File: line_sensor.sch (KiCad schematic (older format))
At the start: 59 parts, among them SW1 SW_DIP_x03, SW2 SW_DIP_x03, SW3 SW_DIP_x03, SW4 SW_DIP_x03, SW5 SW_DIP_x03, SW6 SW_DIP_x03, U1 XH_2, U2 XH_2, U3 XH_2, U4 NJM7800SDL1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

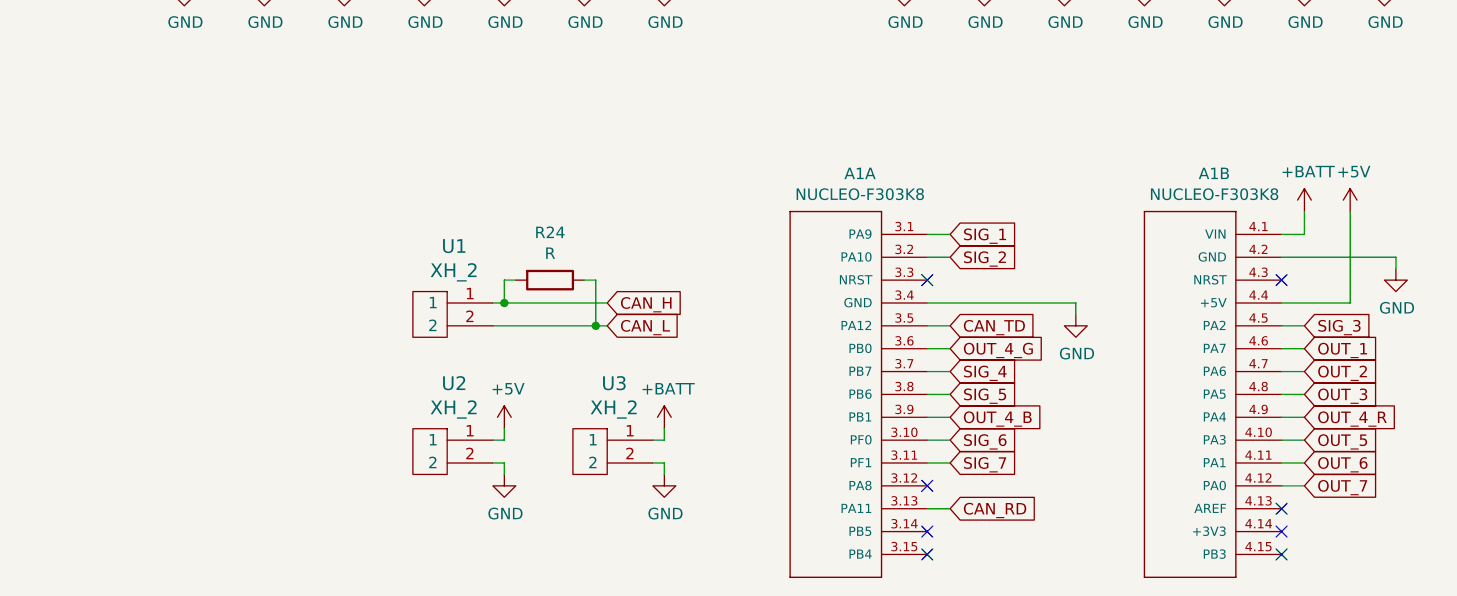
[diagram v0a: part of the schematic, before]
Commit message: update: ライブラリ関係を統合，リネーム
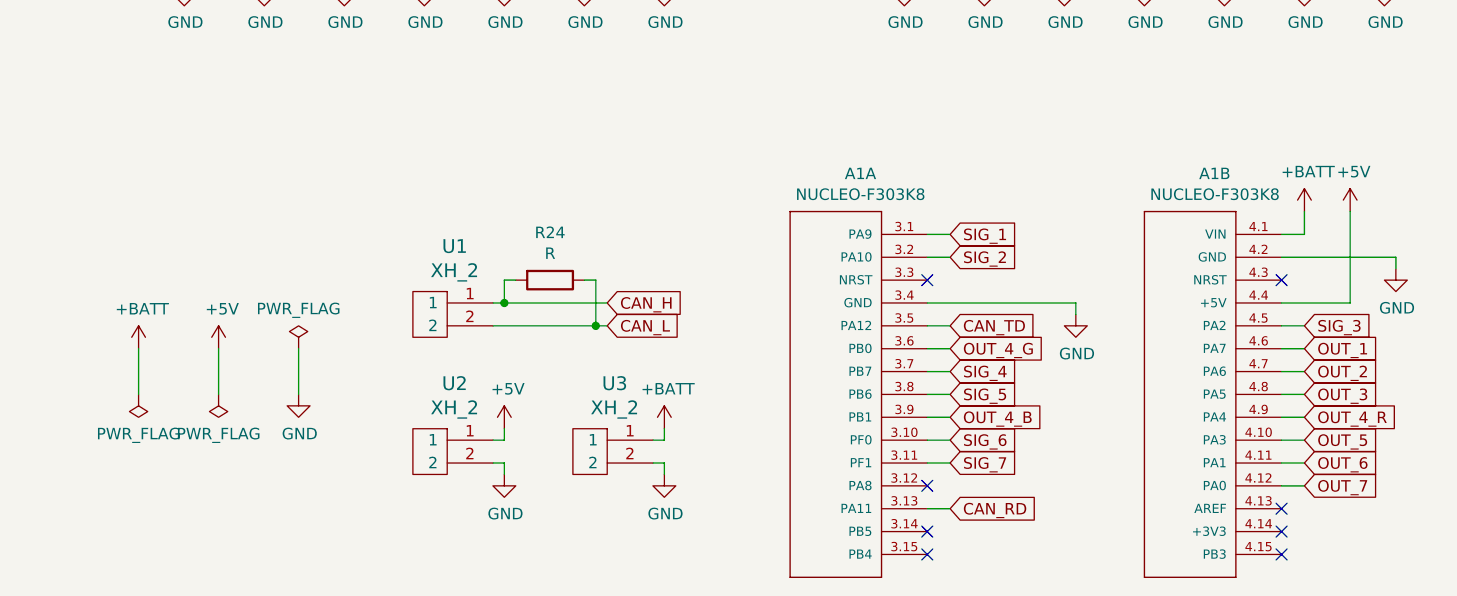
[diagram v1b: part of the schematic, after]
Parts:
- A1: footprint MyFootprint:NUCLEO_F303K8 -> MODULE_NUCLEO-F303K8
- S1, S2, S3, S4, S5, S6, S7: footprint MyFootprint:S9032-02 -> (none)
- U1, U2, U3: footprint MyFootprint:JST_XH_S02B-XH-A_02x2.50mm_Angled -> (none)
- U4: footprint Package_TO_SOT_SMD:TO-252-2 -> (none)
